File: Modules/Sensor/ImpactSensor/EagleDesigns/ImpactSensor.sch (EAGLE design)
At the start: 7 parts

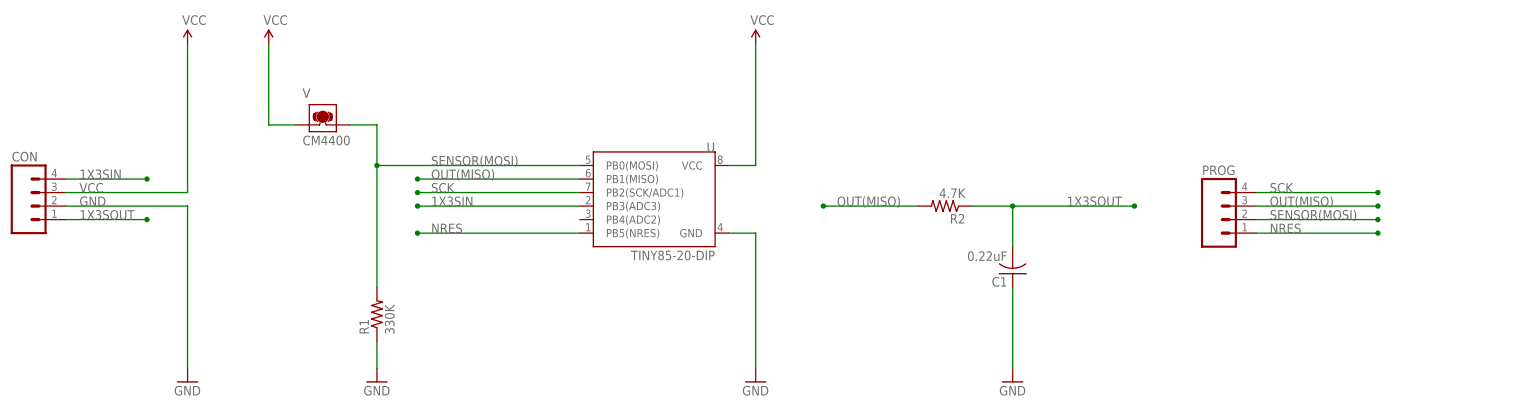
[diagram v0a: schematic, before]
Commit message: added pull-down resistor for Impact Sensor
though we’re currently using the Tilt Sensor’s PCB for our current
design.
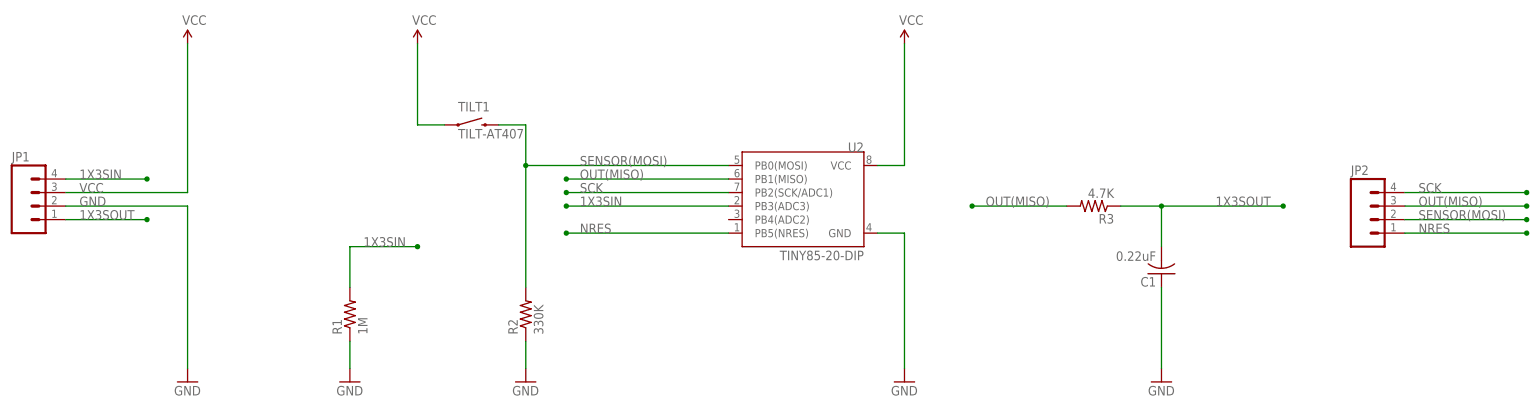
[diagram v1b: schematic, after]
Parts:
- removed PROG: (no value), SparkFun-Connectors:M04PTH
- removed U: TINY85-20-DIP, SparkFun-DigitalIC:ATTINY45TINY85-20-DIP
- removed V: CM4400, sensor-comus-group:CM4400
- added JP2: (no value), SparkFun-Connectors:M04PTH
- added R3: 4.7K, adafruit:R-US_R0603
- added TILT1: TILT-AT407, SparkFun-Electromechanical:TILT-AT407
- added U2: TINY85-20-DIP, SparkFun-DigitalIC:ATTINY45TINY85-20-DIP
- R1: value 330K -> 1M
- R2: value 4.7K -> 330K
- renumbered CON to JP1
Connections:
- net 1X3SIN: now also R1.2, U2.PB3(ADC3); no longer U.PB3(ADC3)
- net 1X3SOUT: now also R3.1; no longer R2.1
- net GND: now also R2.1, U2.GND; no longer U.GND
- net NRES: now also JP2.1, U2.PB5(NRES); no longer PROG.1, U.PB5(NRES)
- net OUT(MISO): now also JP2.3, R3.2, U2.PB1(MISO); no longer PROG.3, R2.2, U.PB1(MISO)
- net SCK: now also JP2.4, U2.PB2(SCK/ADC1); no longer PROG.4, U.PB2(SCK/ADC1)
- net SENSOR(MOSI): now also JP2.2, R2.2, TILT1.2, U2.PB0(MOSI); no longer PROG.2, R1.2, U.PB0(MOSI), V.2
- net VCC: now also TILT1.1, U2.VCC; no longer U.VCC, V.1
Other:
- moved on the sheet: C1, R1, R2
